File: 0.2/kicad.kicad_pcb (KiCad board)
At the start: 2 copper layers, 119.7 x 98.8 mm, 22 parts, among them SW1 SW_PUSH, SW10 SW_PUSH, SW11 SW_PUSH, SW12 SW_PUSH, SW13 SW_PUSH, SW14 SW_PUSH, SW15 SW_PUSH, SW16 SW_PUSH, SW17 SW_PUSH, SW2 SW_PUSH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

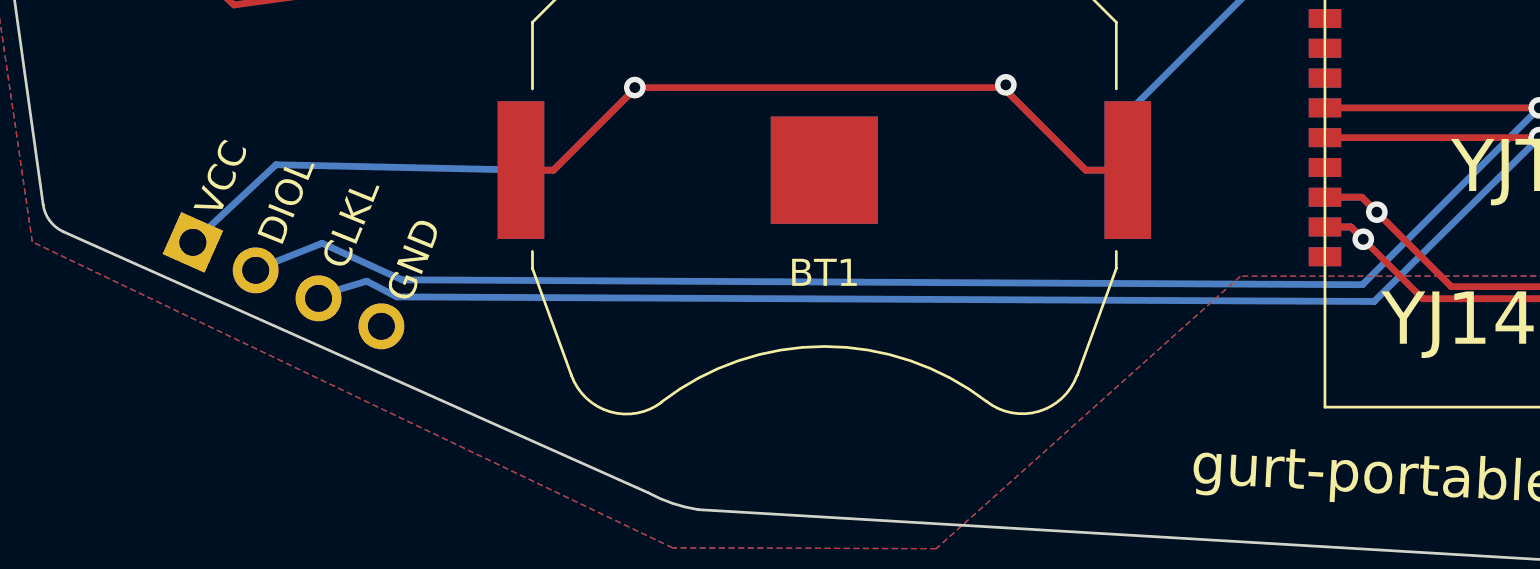
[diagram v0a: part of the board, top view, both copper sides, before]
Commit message: Changed shape of programmer pins
changed the shape of the programmer pins so that the rectangle is for ground
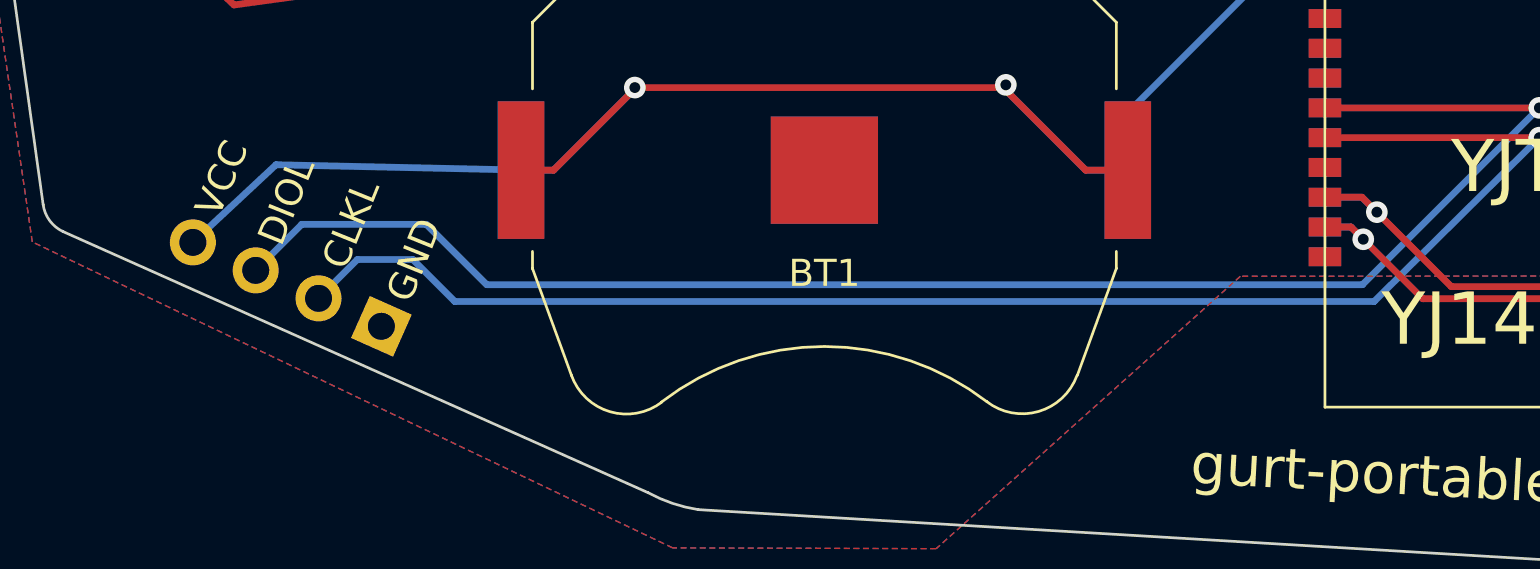
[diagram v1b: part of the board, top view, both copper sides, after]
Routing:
- net DIOL: track 65.6 -> 66.7 mm
- net CLKL: track 62.8 -> 63.8 mm
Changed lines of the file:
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@@
     (fp_line (start 4.04 -8.89) (end 1.5 -8.89) (layer "B.Fab") (width 0.1))
     (fp_line (start 4.04 -5.4) (end 10.04 -5.4) (layer "B.Fab") (width 0.1))
-    (pad "1" thru_hole rect (at 0 0 246) (size 1.7 1.7) (drill 1) (layers *.Cu *.Mask)
+    (pad "1" thru_hole circle (at 0 0 246) (size 1.7 1.7) (drill 1) (layers *.Cu *.Mask)
       (net 1 "VCC") (pinfunction "Pin_1") (pintype "passive"))
     (pad "2" thru_hole oval (at 0 -2.54 246) (size 1.7 1.7) (drill 1) (layers *.Cu *.Mask)
@@
     (pad "3" thru_hole oval (at 0 -5.08 246) (size 1.7 1.7) (drill 1) (layers *.Cu *.Mask)
       (net 21 "CLKL") (pinfunction "Pin_3") (pintype "passive"))
-    (pad "4" thru_hole oval (at 0 -7.62 246) (size 1.7 1.7) (drill 1) (layers *.Cu *.Mask)
+    (pad "4" thru_hole rect (at 0 -7.62 246) (size 1.7 1.7) (drill 1) (layers *.Cu *.Mask)
       (net 2 "GND") (pinfunction "Pin_4") (pintype "passive"))
     (model "${KISYS3DMOD}/Connector_PinHeader_2.54mm.3dshapes/PinHeader_1x04_P2.54mm_Horizontal.wrl"
@@
   (segment (start 142.48384 119.19964) (end 150.40036 119.19964) (width 0.25) (layer "F.Cu") (net 3))
   (via (at 150.40036 119.19964) (size 0.8) (drill 0.4) (layers "F.Cu" "B.Cu") (net 3))
-  (segment (start 103.2914 125.0586) (end 103.1414 125.0586) (width 0.25) (layer "B.Cu") (net 3))
   (segment (start 157.48 119.19964) (end 150.40036 119.19964) (width 0.25) (layer "B.Cu") (net 3))
-  (segment (start 143.86952 125.73048) (end 108.4 125.55) (width 0.25) (layer "B.Cu") (net 3))
-  (segment (start 103.1414 125.0586) (end 103 125.2) (width 0.25) (layer "B.Cu") (net 3))
+  (segment (start 109.3 123.5) (end 104.7 123.5) (width 0.25) (layer "B.Cu") (net 3))
   (segment (start 150.40036 119.19964) (end 143.86952 125.73048) (width 0.25) (layer "B.Cu") (net 3))
-  (segment (start 108.4 125.55) (end 105.45 124.2) (width 0.25) (layer "B.Cu") (net 3))
-  (segment (start 105.45 124.2) (end 103.2914 125.0586) (width 0.25) (layer "B.Cu") (net 3))
+  (segment (start 104.7 123.5) (end 103 125.2) (width 0.25) (layer "B.Cu") (net 3))
+  (segment (start 143.86952 125.73048) (end 111.53048 125.73048) (width 0.25) (layer "B.Cu") (net 3))
+  (segment (start 111.53048 125.73048) (end 109.3 123.5) (width 0.25) (layer "B.Cu") (net 3))
   (segment (start 146.68216 107.75048) (end 114.95048 107.75048) (width 0.25) (layer "F.Cu") (net 4))
   (segment (start 114.95048 107.75048) (end 113.2 106) (width 0.25) (layer "F.Cu") (net 4))
@@
   (via (at 150.4 120.3) (size 0.8) (drill 0.4) (layers "F.Cu" "B.Cu") (net 21))
   (segment (start 150.4 120.3) (end 144.3 126.35) (width 0.25) (layer "B.Cu") (net 21))
-  (segment (start 144.3 126.35) (end 108.215599 126.18) (width 0.25) (layer "B.Cu") (net 21))
-  (segment (start 105.461806 126.091711) (end 105.320406 126.233111) (width 0.25) (layer "B.Cu") (net 21))
+  (segment (start 108.8 124.8) (end 106.753517 124.8) (width 0.25) (layer "B.Cu") (net 21))
+  (segment (start 110.35 126.35) (end 108.8 124.8) (width 0.25) (layer "B.Cu") (net 21))
+  (segment (start 106.753517 124.8) (end 105.320406 126.233111) (width 0.25) (layer "B.Cu") (net 21))
   (segment (start 157.48 120.29946) (end 150.40054 120.29946) (width 0.25) (layer "B.Cu") (net 21))
-  (segment (start 107.1 125.6) (end 105.461806 126.091711) (width 0.25) (layer "B.Cu") (net 21))
-  (segment (start 108.215599 126.18) (end 107.1 125.6) (width 0.25) (layer "B.Cu") (net 21))
+  (segment (start 144.3 126.35) (end 110.35 126.35) (width 0.25) (layer "B.Cu") (net 21))
   (zone (net 2) (net_name "GND") (layers F&B.Cu) (hatch edge 0.508)
     (connect_pads (clearance 0.508))
